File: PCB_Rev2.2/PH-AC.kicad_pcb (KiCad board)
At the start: 2 copper layers, 200 x 100 mm, 51 parts, among them J1 USB_C_Receptacle_USB2.0_16P, J2 Conn_01x03, SW1 SW_Push, SW10 SW_Push, SW2 RotaryEncoder_Switch_MP, SW3 RotaryEncoder_Switch_MP, SW4 SW_Push, SW5 SW_Push, SW6 SW_Push, SW7 SW_Push, SW8 SW_Push, SW9 SW_Push, U1 RP2040, U2 AMS1117-3.3, U3 W25Q16JVSS, Y1 Crystal_GND24

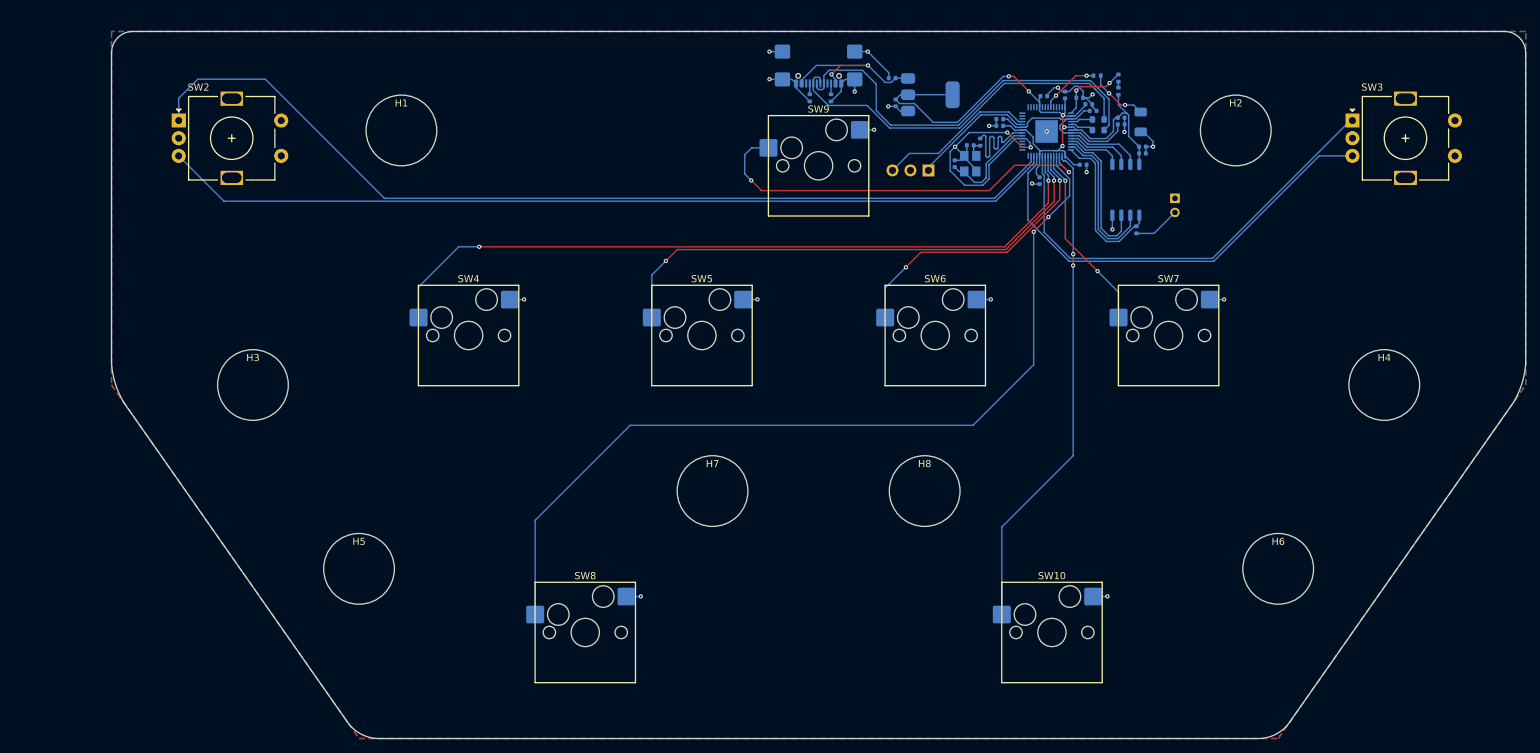
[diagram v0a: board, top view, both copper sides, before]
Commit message: Before merge & open source.
Co-Authored-By: MAltmann <57740314+maltmannx@users.noreply.github.com>
Co-Authored-By: nonameCCC <79012391+nonameCCC@users.noreply.github.com>
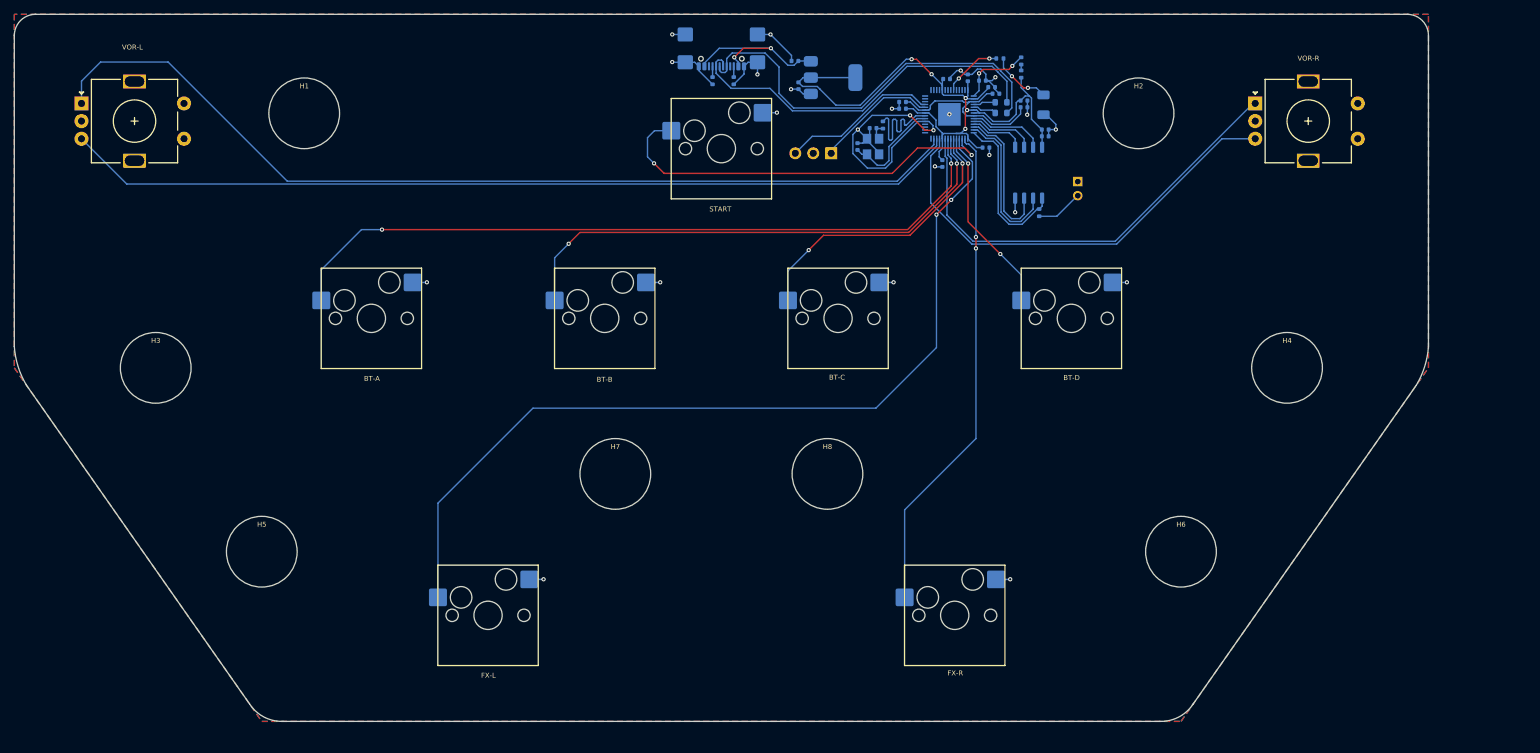
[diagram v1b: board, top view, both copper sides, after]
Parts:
- removed SW1: SW_Push, Connector_PinHeader_2.00mm:PinHeader_1x02_P2.00mm_Vertical
- added JP1: BOOT_SEL, Connector_PinHeader_2.00mm:PinHeader_1x02_P2.00mm_Vertical, B.Cu at (204.2, 74.2)
- U3: value W25Q16JVSS -> W25Q128JVSIQ
- Y1: value Crystal_GND24 -> X322512MSB4SI
- moved BT-A 14.0 mm to (104.2, 93.6)
- moved BT-B 14.0 mm to (137.2, 93.6)
- moved BT-C 14.0 mm to (170.2, 93.6)
- moved BT-D 14.0 mm to (203.2, 93.6)
- moved C1 14.0 mm to (185.6, 59.7)
- moved C10 14.0 mm to (192.0, 60.9)
- moved C11 14.0 mm to (190.7, 60.0)
- moved C12 14.0 mm to (164.2, 57.2)
- moved C13 14.0 mm to (164.7, 60.7)
- moved C14 14.0 mm to (199.6, 66.9)
- moved C15 14.0 mm to (199.6, 67.8)
- moved C17 14.0 mm to (173.0, 69.3)
- moved C18 14.0 mm to (175.2, 66.7)
- moved C2 14.0 mm to (196.6, 62.8)
- moved C3 14.0 mm to (179.4, 63.9)
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- renumbered SW4 to BT-A, SW5 to BT-B, SW6 to BT-C, SW7 to BT-D, SW8 to FX-L, SW10 to FX-R, SW9 to START, SW2 to VOR-L, SW3 to VOR-R
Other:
- board text added: "--Ancade controller for Genshin-impact-like games."
- board text added: "Alt-0191"
- board text added: "MichaelAltmann"
- board text added: "Official Website"
- board text added: "PH-AC"
- board text added: "Team PHDesign"
- board text added: "noname_C"
